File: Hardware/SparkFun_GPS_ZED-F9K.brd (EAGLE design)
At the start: 43.2 x 43.2 mm, 47 parts, among them J1 QWIIC_RIGHT_ANGLE, J4 U.FL, J6 QWIIC_RIGHT_ANGLE, U2 3.3V, U3 UBLOX_ZED_F9K, U4 TRIPLE_BUFFER_74LVC3G07

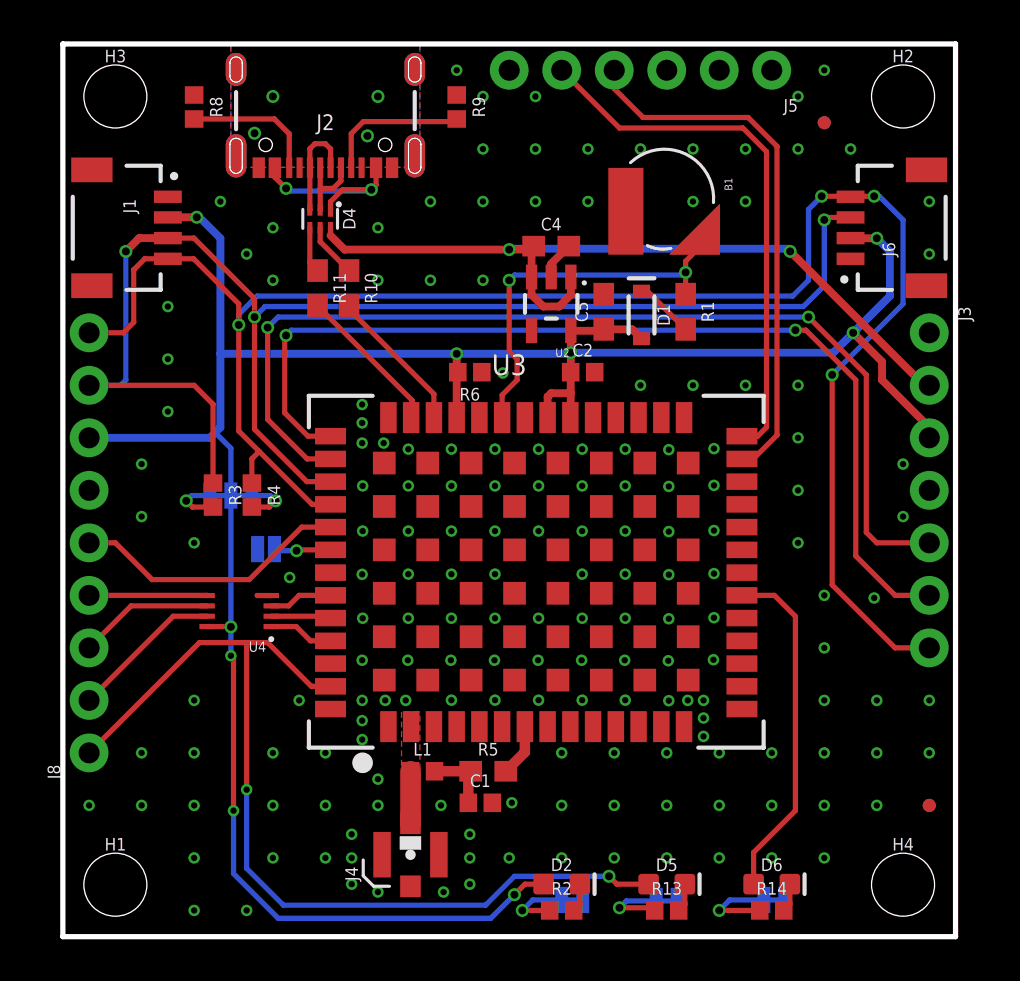
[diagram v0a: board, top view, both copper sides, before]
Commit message: More work to ground pour
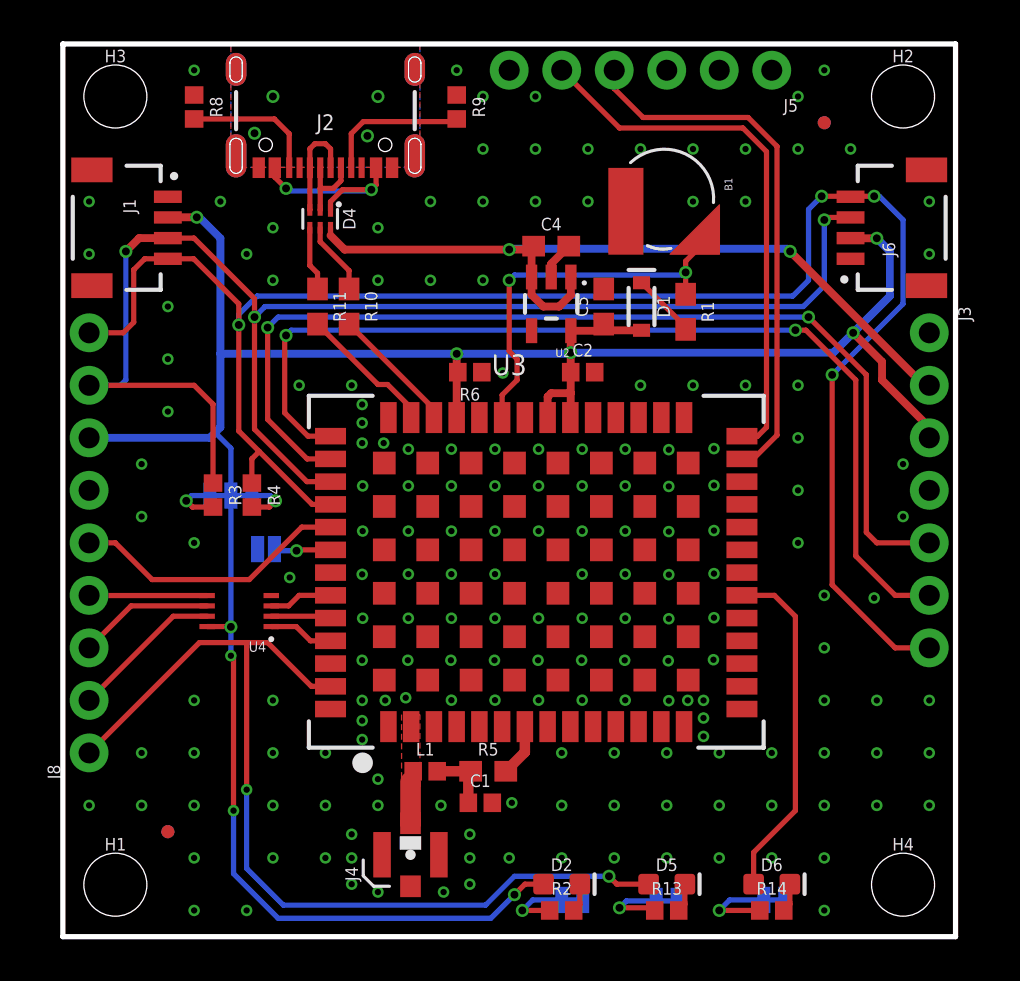
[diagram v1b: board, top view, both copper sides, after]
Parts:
- moved FD2 36.9 mm to (5.08, 5.08)
- moved FD4 36.9 mm to (5.08, 5.08)
- moved R10 0.89 mm to (13.8, 30.5)
- moved R11 0.89 mm to (12.3, 30.5)
- moved D1 0.41 mm to (28.0, 30.5)
- moved C5 0.25 mm to (26.2, 30.5)
- moved L1 0.13 mm to (17.5, 8.00)
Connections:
- removed net SHLD: J2.SHLD1, J2.SHLD2, J2.SHLD3, J2.SHLD4, J2.SHLD5, J2.SHLD6, J2.SHLD7, J2.SHLD8
- new net SHIELD: J2.SHLD1, J2.SHLD2, J2.SHLD3, J2.SHLD4, J2.SHLD5, J2.SHLD6, J2.SHLD7, J2.SHLD8
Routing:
- net N$16: track 2.65 -> 3.54 mm
- net N$17: track 2.23 -> 3.12 mm
- net DMINUS: track 7.11 -> 6.22 mm
- net GND: track 2.53 -> 1.85 mm, vias 173 -> 180
- net 3.3V: track 116.4 -> 115.8 mm
- net DPLUS: track 7.32 -> 6.71 mm
- net RF_IN: track 2.52 -> 2.01 mm

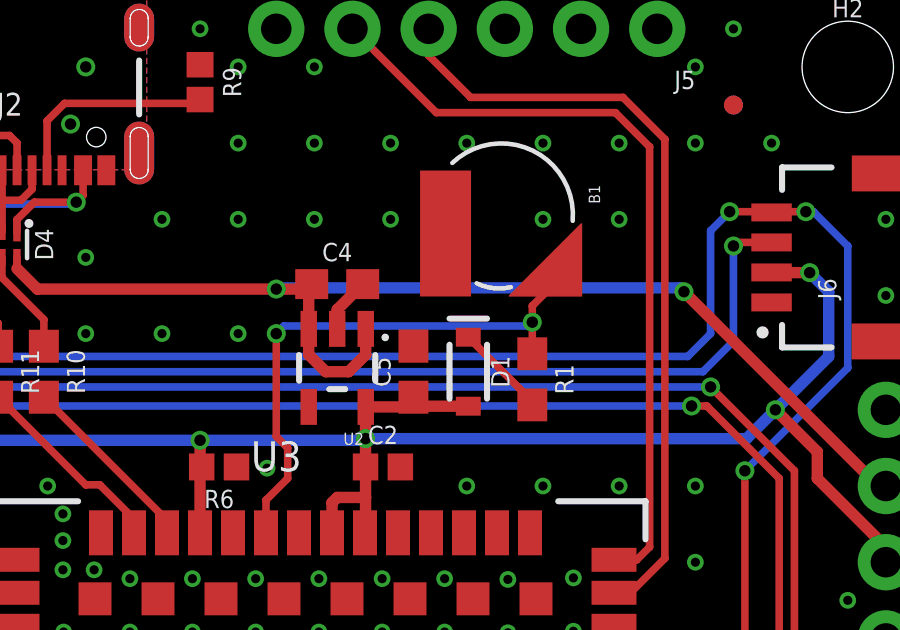
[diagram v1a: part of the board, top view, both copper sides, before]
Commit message: Fixes a few traces
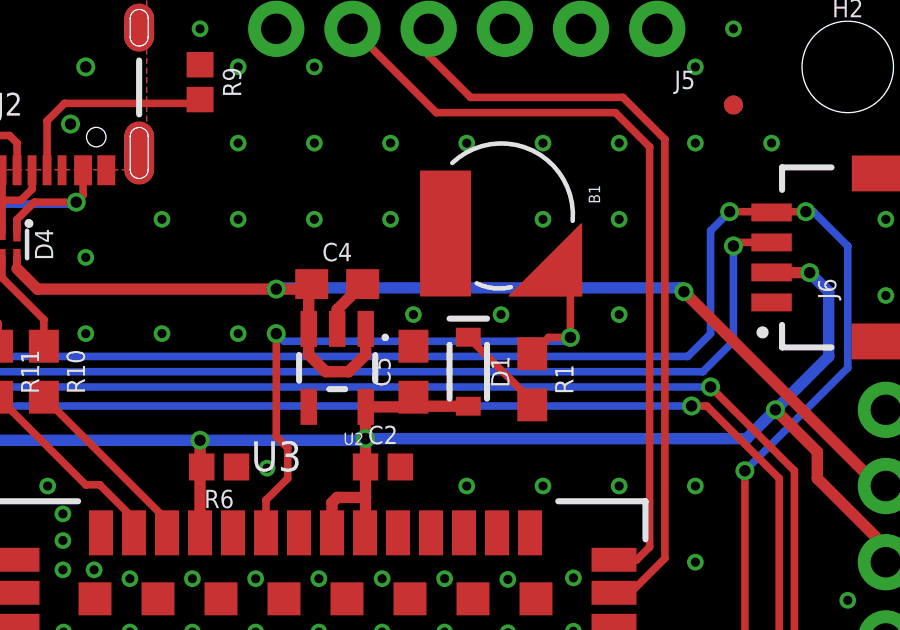
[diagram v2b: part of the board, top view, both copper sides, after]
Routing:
- net V_BATT: track 18.8 -> 20.7 mm
- net GND: vias 180 -> 183
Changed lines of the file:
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@@
 <via x="41.91" y="6.35" extent="1-16" drill="0.3048"/>
 <via x="36.83" y="1.27" extent="1-16" drill="0.3048"/>
+<via x="33.02" y="32.385" extent="1-16" drill="0.3048"/>
+<via x="29.083" y="32.385" extent="1-16" drill="0.3048"/>
+<via x="26.162" y="32.385" extent="1-16" drill="0.3048"/>
 </signal>
 <signal name="3.3V">
@@
 <contactref element="U3" pad="P36"/>
 <wire x1="21.248" y1="25.11" x2="21.248" y2="26.201" width="0.254" layer="1"/>
-<wire x1="30.1244" y1="32.6744" x2="31.115" y2="33.665" width="0.254" layer="1"/>
-<wire x1="30.1244" y1="31.076" x2="30.1244" y2="32.131" width="0.254" layer="1"/>
-<wire x1="30.1244" y1="32.131" x2="30.1244" y2="32.6744" width="0.254" layer="1"/>
 <wire x1="21.248" y1="26.201" x2="21.971" y2="26.924" width="0.254" layer="1"/>
 <wire x1="21.971" y1="26.924" x2="21.971" y2="27.94" width="0.254" layer="1"/>
 <wire x1="21.59" y1="28.321" x2="21.59" y2="31.75" width="0.254" layer="1"/>
 <via x="21.59" y="31.75" extent="1-16" drill="0.381"/>
-<wire x1="21.59" y1="31.75" x2="21.844" y2="32.004" width="0.254" layer="16"/>
-<wire x1="29.9974" y1="32.004" x2="21.844" y2="32.004" width="0.254" layer="16"/>
-<wire x1="29.9974" y1="32.004" x2="30.1244" y2="32.131" width="0.254" layer="16"/>
-<via x="30.1244" y="32.131" extent="1-16" drill="0.381"/>
+<wire x1="31.3944" y1="31.623" x2="31.2674" y2="31.496" width="0.254" layer="16"/>
+<wire x1="21.59" y1="31.75" x2="21.844" y2="31.496" width="0.254" layer="16"/>
+<wire x1="31.2674" y1="31.496" x2="21.844" y2="31.496" width="0.254" layer="16"/>
+<via x="31.3944" y="31.623" extent="1-16" drill="0.381"/>
 <wire x1="21.971" y1="27.94" x2="21.59" y2="28.321" width="0.254" layer="1"/>
+<wire x1="30.1244" y1="31.076" x2="30.6714" y2="31.623" width="0.254" layer="1"/>
+<wire x1="30.6714" y1="31.623" x2="31.3944" y2="31.623" width="0.254" layer="1"/>
+<wire x1="31.3944" y1="31.623" x2="31.3944" y2="33.3856" width="0.254" layer="1"/>
+<wire x1="31.3944" y1="33.3856" x2="31.115" y2="33.665" width="0.254" layer="1"/>
 </signal>
 <signal name="TXO/MISO">

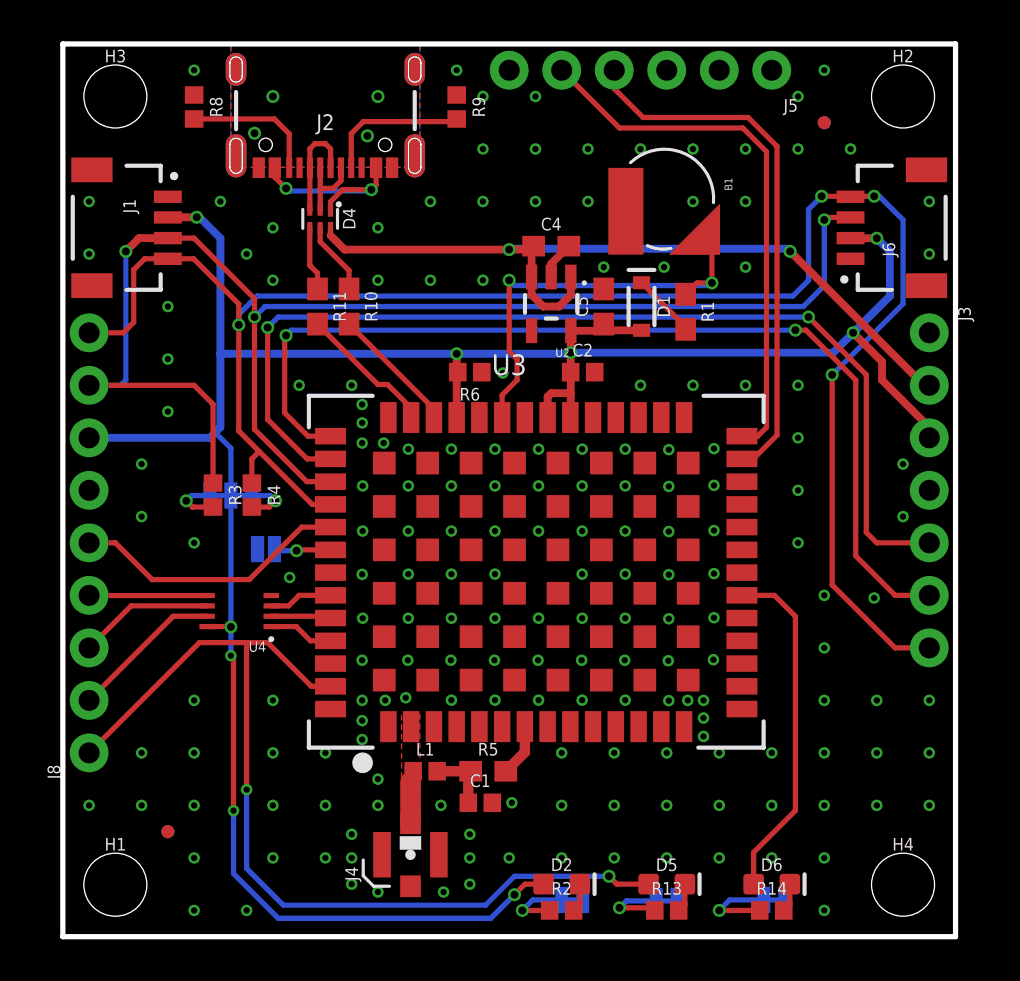
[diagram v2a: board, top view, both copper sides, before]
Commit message: Adds labels to breakout board
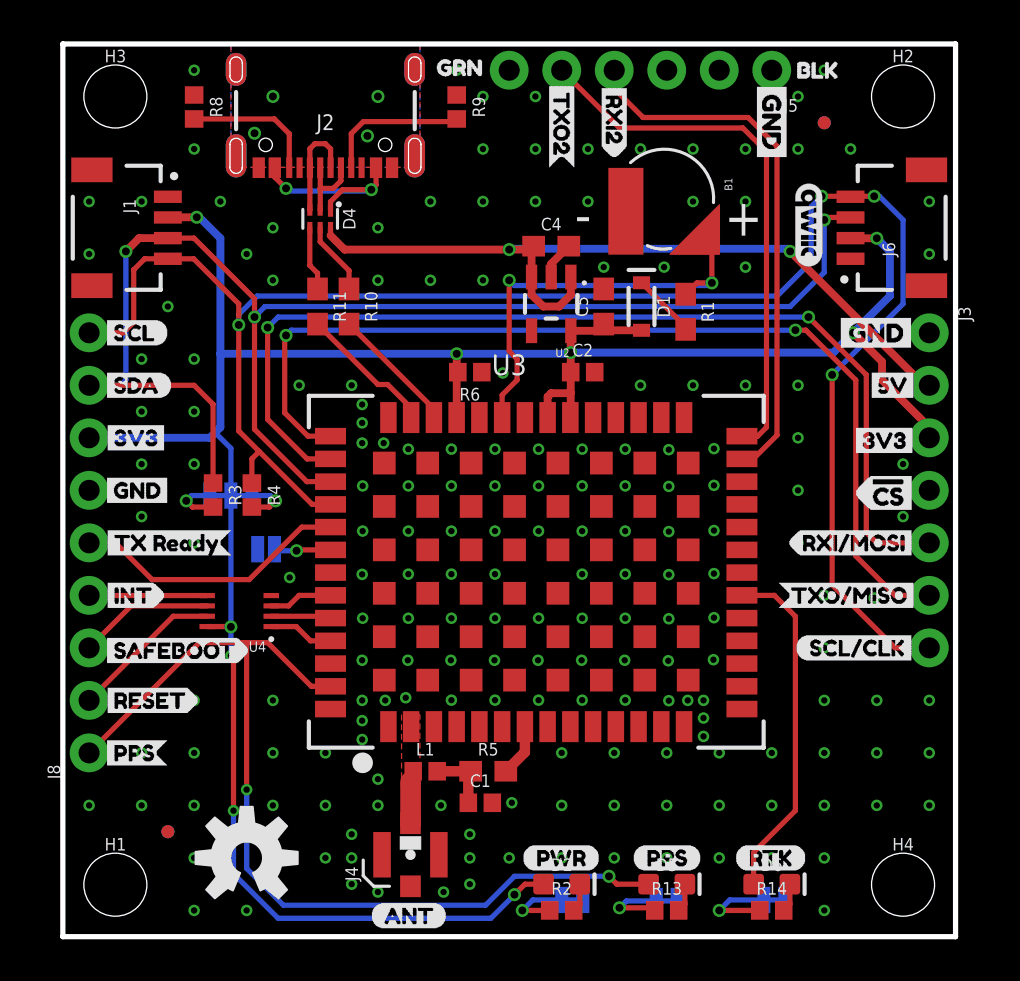
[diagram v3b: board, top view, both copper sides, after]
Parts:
- added LOGO1: SFE_LOGO_NAME_FLAME.2_INCH, SparkFun-Aesthetics:SFE_LOGO_NAME_FLAME_.2
- added LOGO2: QWIIC_LOGO_4MM, SparkFun-Aesthetics:QWIIC_4MM
- added LOGO3: OSHW-LOGOM, SparkFun-Aesthetics:OSHW-LOGO-M
- added U$1: (no value), ALL labels:INT2
- added U$10: (no value), ALL labels:SAFEBOOT1
- added U$11: (no value), scl:SCL0
- added U$12: (no value), I2C Buzzard Labels Small:SDA1
- added U$13: (no value), ALL labels:SCL#CLK7
- added U$14: (no value), rx lables:RXI22
- added U$15: (no value), ALL labels:TXO#MISO6
- added U$16: (no value), ALL labels:TX_READY0
- added U$17, U$20: (no value), Labels:GND-03
- added U$18: (no value), 5V:5V0
- added U$19, U$3: (no value), I2C Buzzard Labels Small:3V32
- added U$2: (no value), ALL labels:PPS4
- added U$21, U$54: (no value), TXR:BLK2
- added U$22, U$8: (no value), ALL labels:RTK9
- added U$23, U$53: (no value), TXR:GRN1
- added U$24: (no value), ALL_LABELS:INT1
- added U$25: (no value), rx lables:TXO21
- added U$26: (no value), Labels:CS#-<]-04
- added U$27: (no value), ALL_LABELS:PPS4
- added U$28: (no value), ALL_LABELS:SAFEBOOT2
- added U$29, U$40: (no value), Labels:3V3-04
- added U$30: (no value), moar:RESET0
- added U$31, U$34, U$41: (no value), Labels:GND-04
- added U$32: (no value), Labels:CS#-[>-04
- added U$33: (no value), Labels:5V
- added U$35: (no value), ALL_LABELS:RXI28
- added U$36: (no value), moar:TXO21
- added U$37: (no value), Labels:SCL-[)
- added U$38: (no value), Labels:SDA-[)
- added U$39: (no value), more_all_labels:TXR0
- added U$4, U$47: (no value), ALL labels:PPS8
- added U$42: (no value), more_all_labels:RXI#MOSI1
- added U$43: (no value), more_all_labels:TXO#MISO2
- added U$44: (no value), more_all_labels:SCL#CLK3
- added U$45: (no value), more_all_labels:SPI4
- added U$46: (no value), Labels:I_SUPER2_C-()-04
- added U$48, U$5: (no value), ALL labels:PWR10
- added U$49: (no value), ant:ANT0
- added U$50: (no value), NEO_GPS_board_silk_FINAL#03#jpg:NEO_GPS_BOARD_SILK_FINAL#03#JPG
- added U$51: (no value), zed:ZED#F9R0
- added U$52: (no value), zed:U#BLOX1
- added U$6: (no value), I2C Buzzard Labels Small:GND3
- added U$7: (no value), ALL labels:RESET3
- added U$9: (no value), ALL labels:RXI#MOSI5
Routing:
- net GND: vias 183 -> 188
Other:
- board text added: "+"
- board text added: "-"
- board text added: "Units In Inches"
